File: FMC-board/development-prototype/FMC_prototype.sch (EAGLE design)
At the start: 68 parts, among them J1 DC_POWER_JACK-PJ-102AH, J2 PJ-102AH, U1 TPS79333

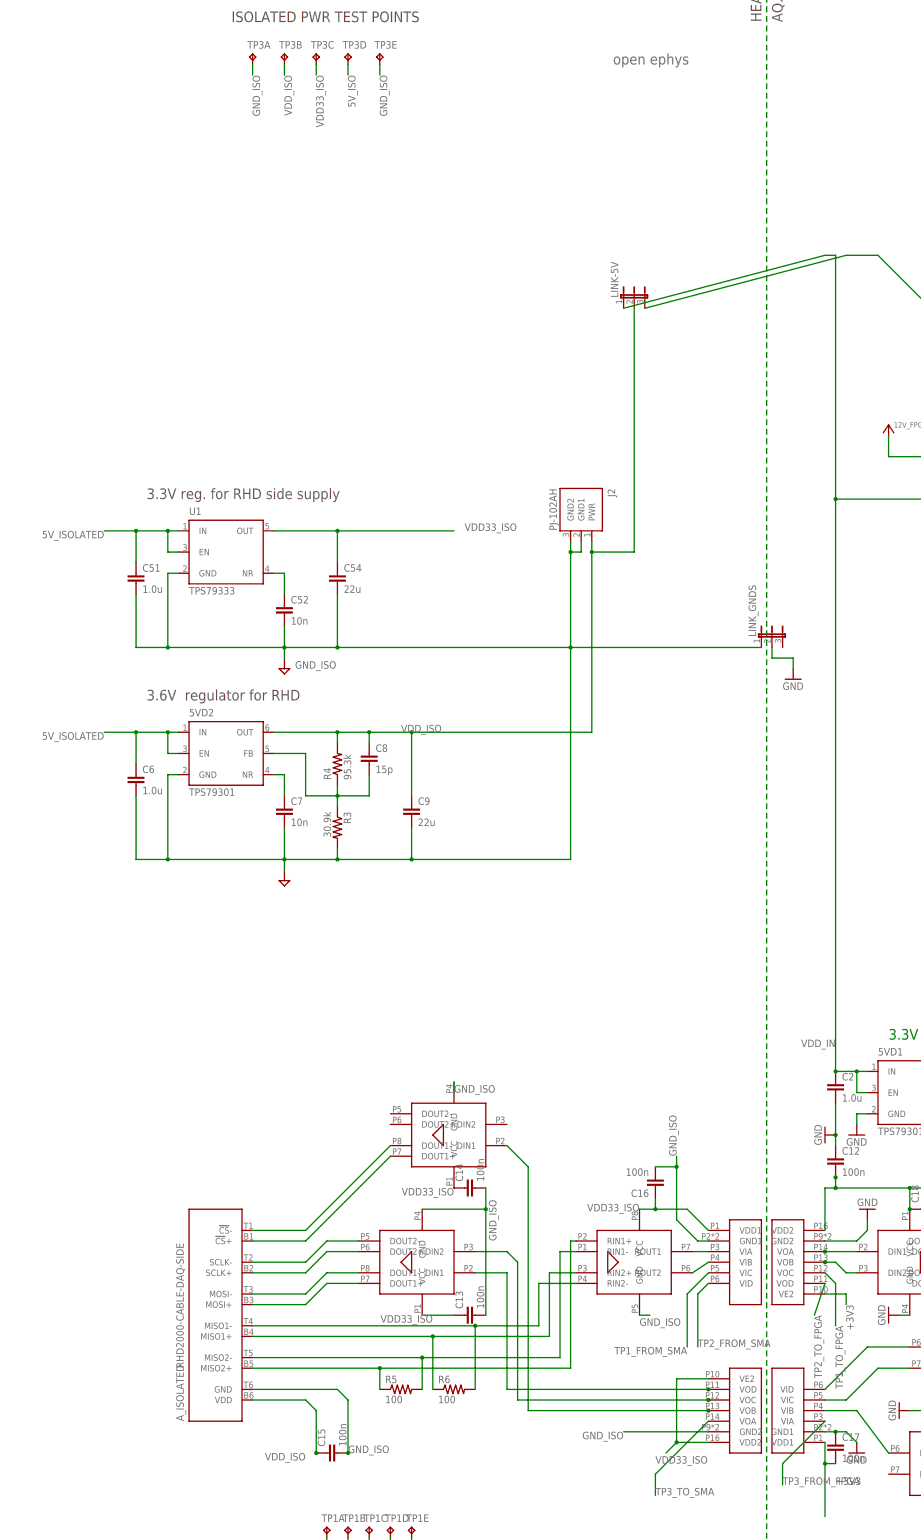
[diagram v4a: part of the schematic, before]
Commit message: Looks like isolated 5V was wired to output of isolated 3.6V regulator and input is floating to both isolated regulators. In the middle of fixing that.
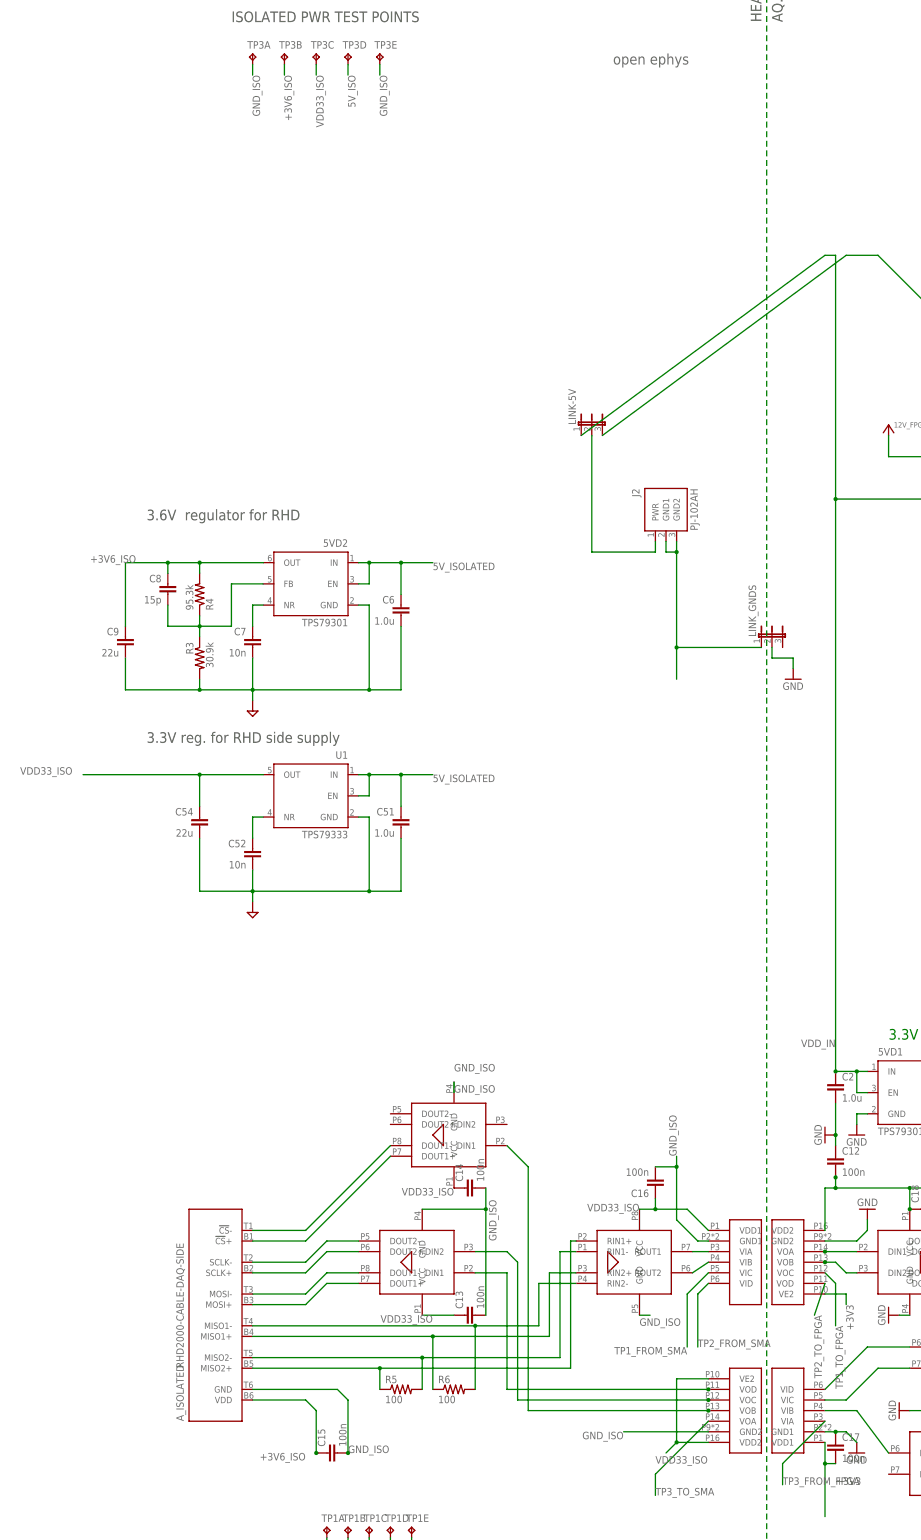
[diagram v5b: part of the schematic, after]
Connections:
- removed net VDD_ISO: 5VD2.OUT, A_ISOLATED.VDD, C15.1, C8.1, C9.1, J2.PWR, LINK-5V.2, R4.2, TP3B.TP
- new net +3V6_ISO: 5VD2.OUT, A_ISOLATED.VDD, C15.1, C8.1, C9.1, R4.2, TP3B.TP
- new net N$3: C51.2, C52.2, C54.2, U1.GND
- new net N$4: J2.GND1, J2.GND2, LINK_GNDS.1
- new net N$5: J2.PWR, LINK-5V.2
- net GND_ISO: no longer C51.2, C52.2, C54.2, J2.GND1, J2.GND2, LINK_GNDS.1, U1.GND
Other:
- moved on the sheet: 5VD2, C51, C52, C54, C6, C7, C8, C9, J2, LINK-5V, R3, R4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

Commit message: More or less done checking power section of schematic.
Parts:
- removed 5VD1: TPS79301, RHD2000_eval_board:TPS79301
- removed C4: 15p, RHD2000_eval_board:C_0603
- added R7: 10k, RHD2000_eval_board:R_0603
- added U2: TPS79333, jonnew:TPS79333
- R1: value 30.9k -> 10k
- R2: value 95.3k -> 10k
- U$20: value PDS1 -> PDS1-S12-S5-S; device open-ephys:PDS1 -> jonnew:PDS1
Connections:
- net N$1 renamed +5V0_ISO-PRE
- net VDD33_ISO renamed +3V3_ISO
- removed net 5V_ISO: TP3D.TP
- removed net 5V_ISOLATED: 5VD2.EN, 5VD2.IN, C51.1, C6.1, U1.EN, U1.IN
- removed net N$35: 5VD1.FB, C4.2, R1.1, R2.1
- removed net N$4: J2.GND1, J2.GND2, LINK_GNDS.1
- new net +5V0_ISO: 5VD2.EN, 5VD2.IN, C51.1, C6.1, J2.PWR, LINK-5V.2, TP3D.TP, U1.EN, U1.IN
- new net N$1: R2.2, U$10.RIN1-
- net +3V3: now also U2.OUT; no longer 5VD1.OUT, C4.1, R2.2
- net GND: now also LINK_GNDS.3, R2.1, R7.1, U2.GND; no longer 5VD1.GND, LINK_GNDS.2, R1.2
- net GND_ISO: now also C51.2, C52.2, C54.2, J2.GND1, J2.GND2, LINK_GNDS.2, R1.1, U1.GND
- net N$3: now also R7.2, U$10.RIN1+; no longer C51.2, C52.2, C54.2, U1.GND
- net N$33: now also U2.NR; no longer 5VD1.NR
- net N$5: now also R1.2, U$9.DIN2; no longer J2.PWR, LINK-5V.2
- net VDD_IN: now also U2.EN, U2.IN; no longer 5VD1.EN, 5VD1.IN
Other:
- note added: "12V-TO-5V ISOLATED DC-DC"
- note removed: "12V to 5V DC-Dc"
- moved on the sheet: 5VD2, 5VD4, C1, C12, C2, C20, C21, C22, C23, C3, C5, C51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

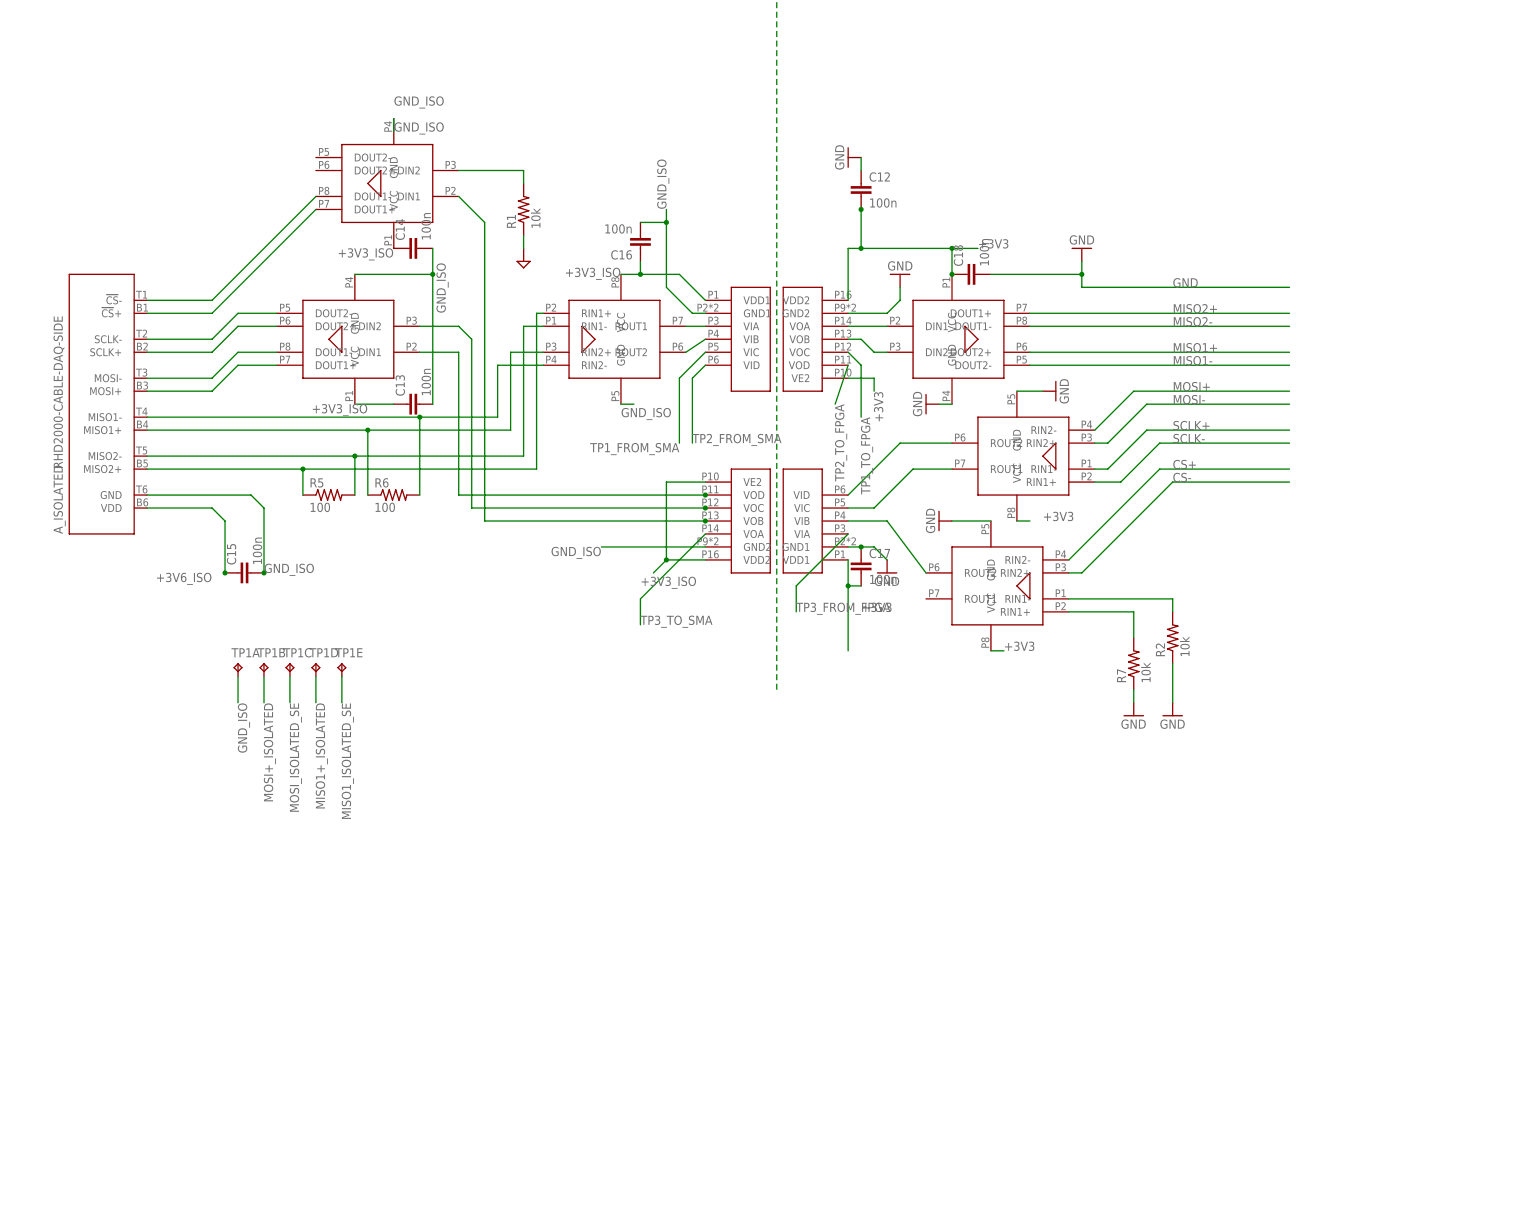
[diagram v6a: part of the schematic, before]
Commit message: Started working on digital ports.
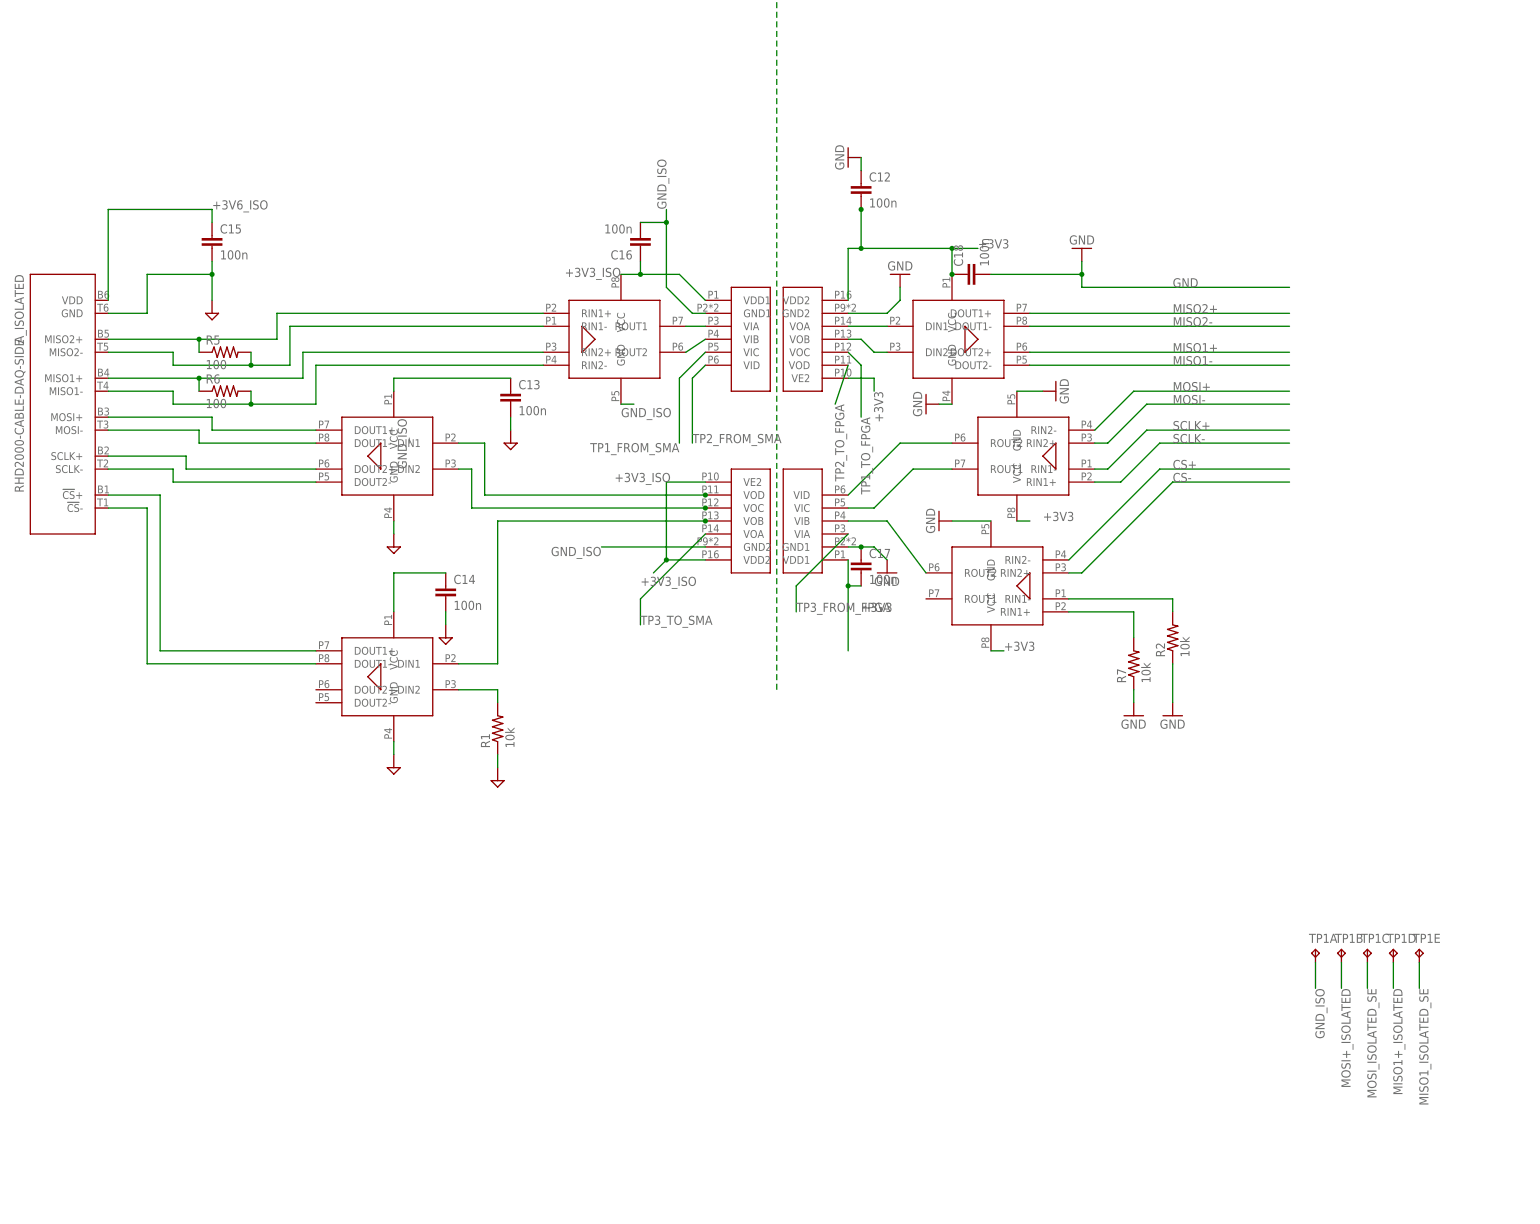
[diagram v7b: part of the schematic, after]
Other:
- moved on the sheet: A_ISOLATED, C13, C14, C15, R1, R5, R6, TP1A, TP1B, TP1C, TP1D, TP1E

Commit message: More digital port cleanup.
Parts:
- U$10, U$6, U$8: value ADN4664 -> (none); device open-ephys:ADN4664 -> jonnew:ADN4664_SOIC
- U$3, U$7, U$9: value ADN4663 -> (none); device open-ephys:ADN4663 -> jonnew:ADN4663_SOIC
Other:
- moved on the sheet: C13, C14, C15
